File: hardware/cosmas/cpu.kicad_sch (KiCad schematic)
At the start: 1 part, among them U3 ESP32-DEVKIT-V1

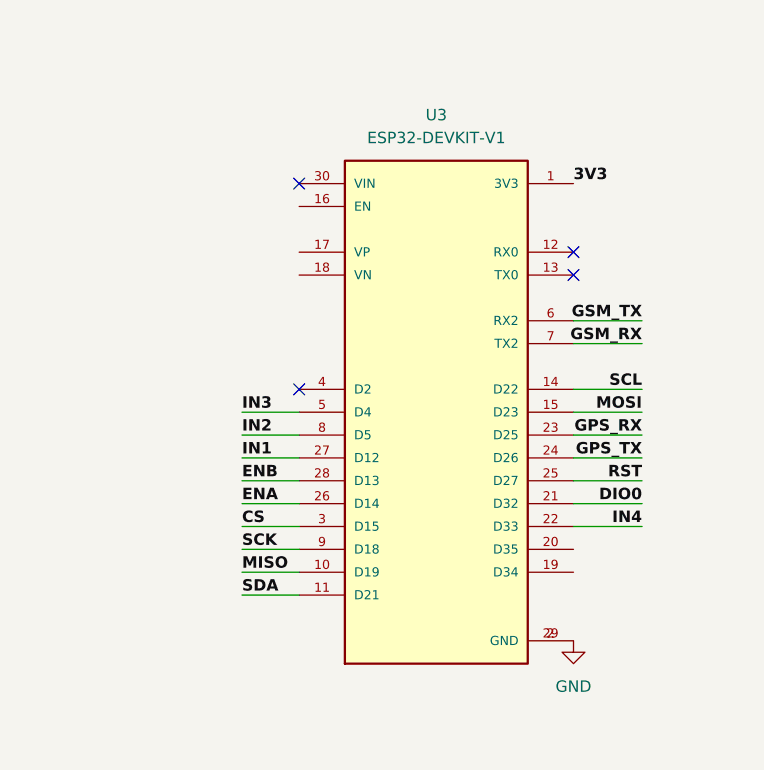
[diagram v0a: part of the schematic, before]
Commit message: updates net labels
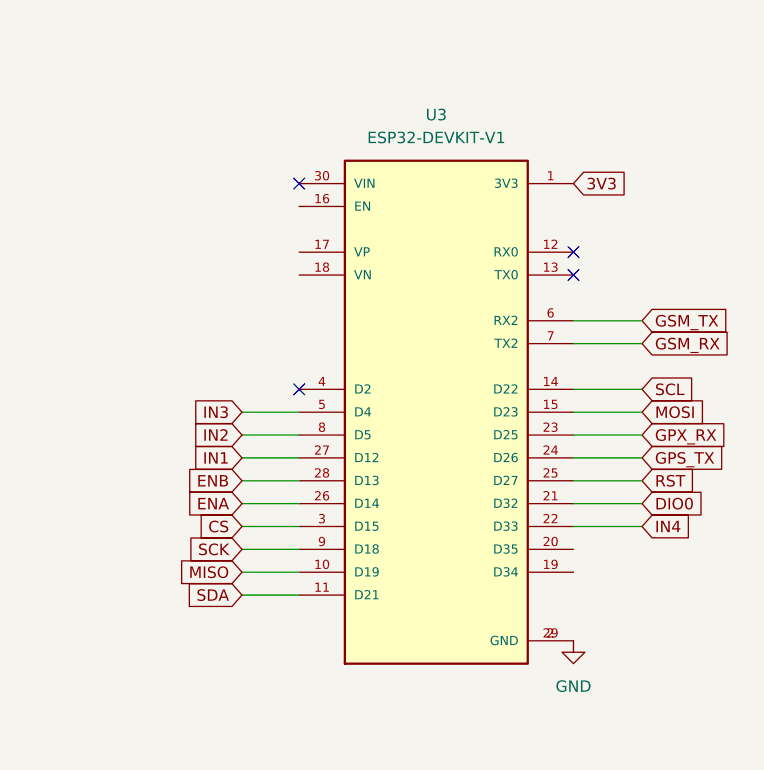
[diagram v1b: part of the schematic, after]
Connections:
- net GPS_RX renamed GPX_RX

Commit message: adds OBC PCB
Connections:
- net BUZZER: now reaches U3.4 (D2)
- net GPX_RX renamed GPS_RX
- no-connect marks 4 -> 3
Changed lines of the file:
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@@
-	)
-	(no_connect
-		(at 129.54 96.52)
 	)
 	(no_connect
@@
 		(pts
 			(xy 123.19 119.38) (xy 129.54 119.38)
+		)
+		(stroke
+			(width 0)
+			(type default)
+		)
+	)
+	(wire
+		(pts
+			(xy 123.19 96.52) (xy 129.54 96.52)
 		)
 		(stroke
@@
 				(thickness 1.778)
 				(bold yes)
+			)
+		)
+	)
+	(global_label "BUZZER"
+		(shape input)
+		(at 123.19 96.52 180)
+		(fields_autoplaced yes)
+		(effects
+			(font
+				(size 1.27 1.27)
+			)
+			(justify right)
+		)
+		(property "Intersheetrefs" "${INTERSHEET_REFS}"
+			(at 112.7663 96.52 0)
+			(effects
+				(font
+					(size 1.27 1.27)
+				)
+				(justify right)
+				(hide yes)
 			)
 		)
@@
 		)
 	)
-	(global_label "GPX_RX"
+	(global_label "GPS_RX"
 		(shape input)
 		(at 167.64 101.6 0)
